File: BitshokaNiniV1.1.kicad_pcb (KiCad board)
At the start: 4 copper layers, 56.5 x 99.8 mm, 154 parts, among them J1 54-00164, J2 TC2030-IDC, J3 Conn_01x04, J4 Conn_01x06, J5 USB_C_Receptacle_USB2.0, J6 Conn_01x04, J7 Conn_01x04, Q1 MMBT3906, Q3 MMBT3906, SW1 GT-TC029B-H025-L1N, SW2 GT-TC029B-H025-L1N, T1 net-tie, U10 EMC2101, U2 TPS546D24ARVFR, U23 LM358, U3 RT9080-33GJ5, U4 ESP32-S3-WROOM-1, U5 SPX3819M5-L-1-8, U7 25MHz, U9 SN74AVC4T774

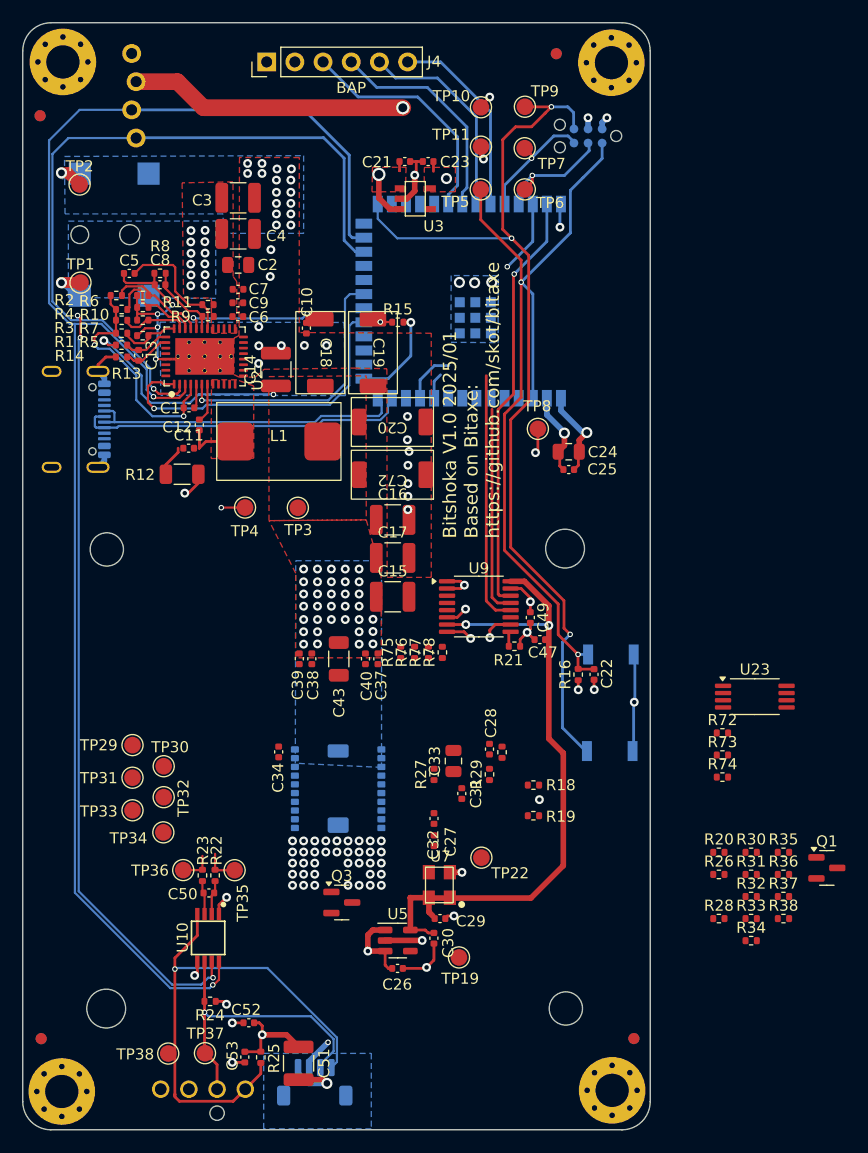
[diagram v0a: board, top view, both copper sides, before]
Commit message: All components placed
Went through TI schematic and layout checklist.
All components placed and initial DRC
Need thermal vias on KF1950 and also better layout (so not so many errors)
Need to do silk
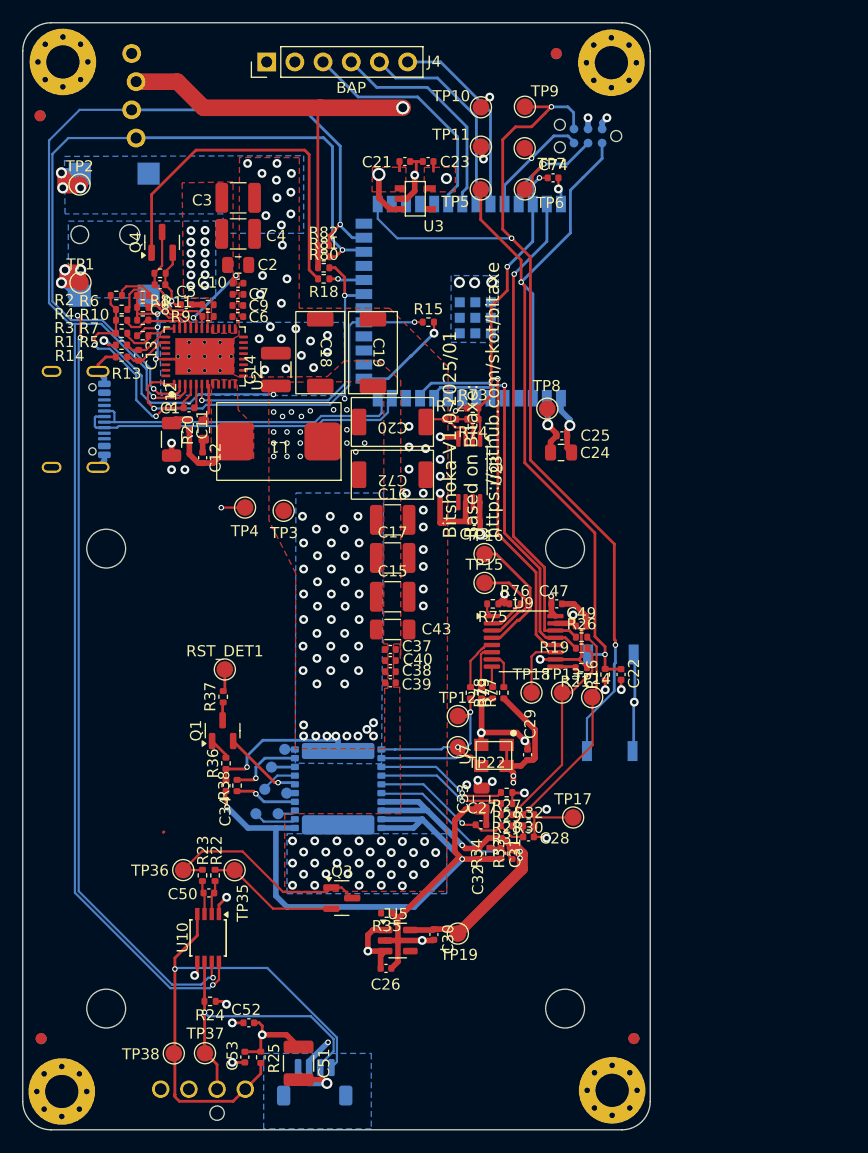
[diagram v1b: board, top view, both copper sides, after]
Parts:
- removed TP29, TP30, TP31, TP32, TP33, TP34: TestPoint, TestPoint:TestPoint_Pad_D1.5mm
- added C73: 0.1uF, Capacitor_SMD:C_0402_1005Metric, F.Cu at (117.9, 92.5)
- added C74: 0.1uF, Capacitor_SMD:C_0402_1005Metric, F.Cu at (125.0, 61.5)
- added Q4: MMBT2222A, Package_TO_SOT_SMD:SOT-23, F.Cu at (89.8, 67.3)
- added R79: 0, Resistor_SMD:R_0402_1005Metric, F.Cu at (117.5, 107.9)
- added R80: 4.7k, Resistor_SMD:R_0402_1005Metric, F.Cu at (104.3, 69.6)
- added R81: 4.7k, Resistor_SMD:R_0402_1005Metric, F.Cu at (104.3, 68.6)
- added R82: 4.7k, Resistor_SMD:R_0402_1005Metric, F.Cu at (104.3, 67.6)
- added RST_DET1: TestPoint, TestPoint:TestPoint_Pad_D1.5mm, F.Cu at (95.4, 105.8)
- added TP12: TestPoint, TestPoint:TestPoint_Pad_D1.5mm, F.Cu at (116.4, 110.0)
- added TP13: TestPoint, TestPoint:TestPoint_Pad_D1.5mm, F.Cu at (125.8, 107.9)
- added TP14: TestPoint, TestPoint:TestPoint_Pad_D1.5mm, F.Cu at (128.5, 108.3)
- added TP15: TestPoint, TestPoint:TestPoint_Pad_D1.5mm, F.Cu at (118.8, 98.0)
- added TP16: TestPoint, TestPoint:TestPoint_Pad_D1.5mm, F.Cu at (118.8, 95.4)
- added TP17: TestPoint, TestPoint:TestPoint_Pad_D1.5mm, F.Cu at (126.8, 119.1)
- added TP18: TestPoint, TestPoint:TestPoint_Pad_D1.5mm, F.Cu at (123.0, 107.9)
- added TP20: TestPoint, TestPoint:TestPoint_Pad_D1.0mm, B.Cu at (100.8, 113.0)
- added TP21: TestPoint, TestPoint:TestPoint_Pad_D1.0mm, B.Cu at (99.6, 114.6)
- added TP23: TestPoint, TestPoint:TestPoint_Pad_D1.0mm, B.Cu at (99.0, 116.6)
- added TP24: TestPoint, TestPoint:TestPoint_Pad_D1.0mm, B.Cu at (101.0, 116.9)
- added TP25: TestPoint, TestPoint:TestPoint_Pad_D1.0mm, B.Cu at (100.2, 118.8)
- added TP26: TestPoint, TestPoint:TestPoint_Pad_D1.0mm, B.Cu at (98.2, 118.8)
- R1: value 8.25k -> 4.64k
- R10: value 68.1k -> 0
- R18: value 0 -> 100
- R20: footprint Resistor_SMD:R_0402_1005Metric -> Resistor_SMD:R_0603_1608Metric
- R32: value 390 -> 400
- R33: value 27.5 -> 33
- R34: value 33 -> 27
- R5: value 14.7k -> 4.64k
- R73: value 40k -> 0
- U7: value 25MHz -> 24MHz
- moved R20 60.0 mm to (93.5, 84.2), turned to 90 degrees
- moved Q1 55.8 mm to (95.2, 111.3), turned to 90 degrees
- moved R37 53.6 mm to (95.2, 108.3), turned to 90 degrees
- moved R36 51.2 mm to (95.5, 114.3), turned to 90 degrees
- moved R38 50.7 mm to (96.5, 116.3), turned to 90 degrees
- moved R18 49.4 mm to (104.3, 70.6)
- moved R74 39.3 mm to (117.8, 83.2), turned to 180 degrees
- moved R73 38.5 mm to (117.7, 82.2)
- moved R72 37.4 mm to (115.7, 83.2)
- moved R35 36.2 mm to (110.0, 127.8), turned to 180 degrees
- moved U23 32.8 mm to (117.4, 87.9), turned to -90 degrees
- moved R34 24.8 mm to (119.3, 122.4), turned to 90 degrees
- moved R26 24.7 mm to (127.5, 102.9)
- moved R31 22.5 mm to (120.8, 119.9), turned to 180 degrees
- moved R33 22.3 mm to (121.3, 122.4), turned to 90 degrees
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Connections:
- C12 pad 1: Net-(U2-BOOT) -> Net-(C12-Pad1)
- C26 pad 2: GND -> /KF1950/LDO_GND
- C28 pad 1: /KF1950/1V8 -> GND
- C29 pad 2: /KF1950/1V2 -> /KF1950/1V8
- C30 pad 2: GND -> /KF1950/LDO_GND
- C33 pad 2: /KF1950/VDD -> /VDD
- C34 pad 2: /KF1950/VDD -> /VDD
- C37 pad 1: /KF1950/VDD -> /VDD
- C38 pad 1: /KF1950/VDD -> /VDD
- C39 pad 1: /KF1950/VDD -> /VDD
- C40 pad 1: /KF1950/VDD -> /VDD
- C43 pad 1: /KF1950/VDD -> /VDD
- R17 pad 1: /KF1950/ESP_RXD -> GND
- R17 pad 2: /KF1950/TXD -> Net-(U9-A4)
- R18 pad 1: /KF1950/TXD_1V8 -> /ESP32//TPS_EN
- R18 pad 2: /KF1950/RXD -> Net-(Q4-B)
- R19 pad 1: /KF1950/ESP_TXD -> /ESP_TXD
- R20 pad 1: /KF1950/RST_1V8 -> Net-(C12-Pad1)
- R20 pad 2: /KF1950//RST -> Net-(U2-BOOT)
- R26 pad 1: /KF1950/ESP_RST -> /ESP_RST
- R32 pad 2: /KF1950/1V8 -> GND
- R36 pad 1: /KF1950/VDD -> /VDD
- U4 pad 10: /TX -> /ESP_TXD
- U4 pad 11: /RX -> /ESP_RXD
- U4 pad 22: unconnected-(U4-GPIO14/TOUCH14/ADC2_CH3/FSPIWP/FSPIDQS/SUBSPIWP-Pad22) -> /ESP32//TPS_EN
- U4 pad 39: /RST -> /ESP_RST
- U5 pad 2: GND -> /KF1950/LDO_GND
- U7 pad 4: /KF1950/1V2 -> /KF1950/1V8
- U8 pad 12: unconnected-(U8-GND-Pad12) -> Net-(TP26-Pad1)
- U8 pad 13: unconnected-(U8-DIR-Pad13) -> Net-(TP25-Pad1)
- U8 pad 15: unconnected-(U8-0.9V-Pad15) -> Net-(TP24-Pad1)
- U8 pad 17: unconnected-(U8-RXD-Pad17) -> Net-(TP23-Pad1)
- U8 pad 18: unconnected-(U8-CTSI-Pad18) -> Net-(TP21-Pad1)
- U8 pad 20: unconnected-(U8-CLK-Pad20) -> Net-(TP20-Pad1)
- U8 pad 21: /KF1950/VDD -> /VDD
- U9 pad 11: unconnected-(U9-B4-Pad11) -> Net-(U9-B4)
- U9 pad 12: /KF1950/ESP_RXD -> /ESP_RXD
- U9 pad 13: /KF1950/ESP_TXD -> /ESP_TXD
- U9 pad 14: /KF1950/ESP_RST -> /ESP_RST
- U9 pad 6: GND -> Net-(U9-A4)
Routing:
- net /KF1950/LDO_GND: track 0.00 -> 75.8 mm, vias 0 -> 3
- net /KF1950/1V8: track 0.00 -> 74.1 mm, vias 0 -> 6
- net (no net): track 59.0 -> 0.07 mm, vias 2 -> 0
- net /ESP_RST: track 0.00 -> 43.9 mm, vias 0 -> 1
- net /VDD: track 20.1 -> 62.7 mm, vias 36 -> 73
- net /RST: track 38.2 -> 0.00 mm, vias 1 -> 0
- net /ESP_RXD: track 0.00 -> 34.6 mm, vias 0 -> 1
- net /ESP_TXD: track 0.00 -> 34.4 mm, vias 0 -> 1
- net Net-(Q4-B): track 0.00 -> 32.8 mm
- net GND: track 71.9 -> 94.9 mm, vias 93 -> 102
- net /KF1950/ESP_RXD: track 22.8 -> 0.00 mm
- net /KF1950//RST: track 0.00 -> 20.5 mm
- net Net-(U4-GPIO2/TOUCH2/ADC1_CH1): track 6.63 -> 26.6 mm, vias 1 -> 2
- net /KF1950/ESP_TXD: track 18.8 -> 0.00 mm
- net /KF1950/RXD: track 0.04 -> 18.6 mm
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- added copper zone on In2.Cu, net /VDD
- added copper zone on B.Cu, net unconnected-(J7-MountPin-PadMP)
- removed copper zone on B.Cu, net unconnected-(J7-MountPin-PadMP)_1
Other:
- board text added: "This area is solder mask free for heatsinking with 14 x 14mm Raspberry PI heatsink"

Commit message: Silk Done
Still need to fix up heatsink vias on ASIC and paste layer for thermal
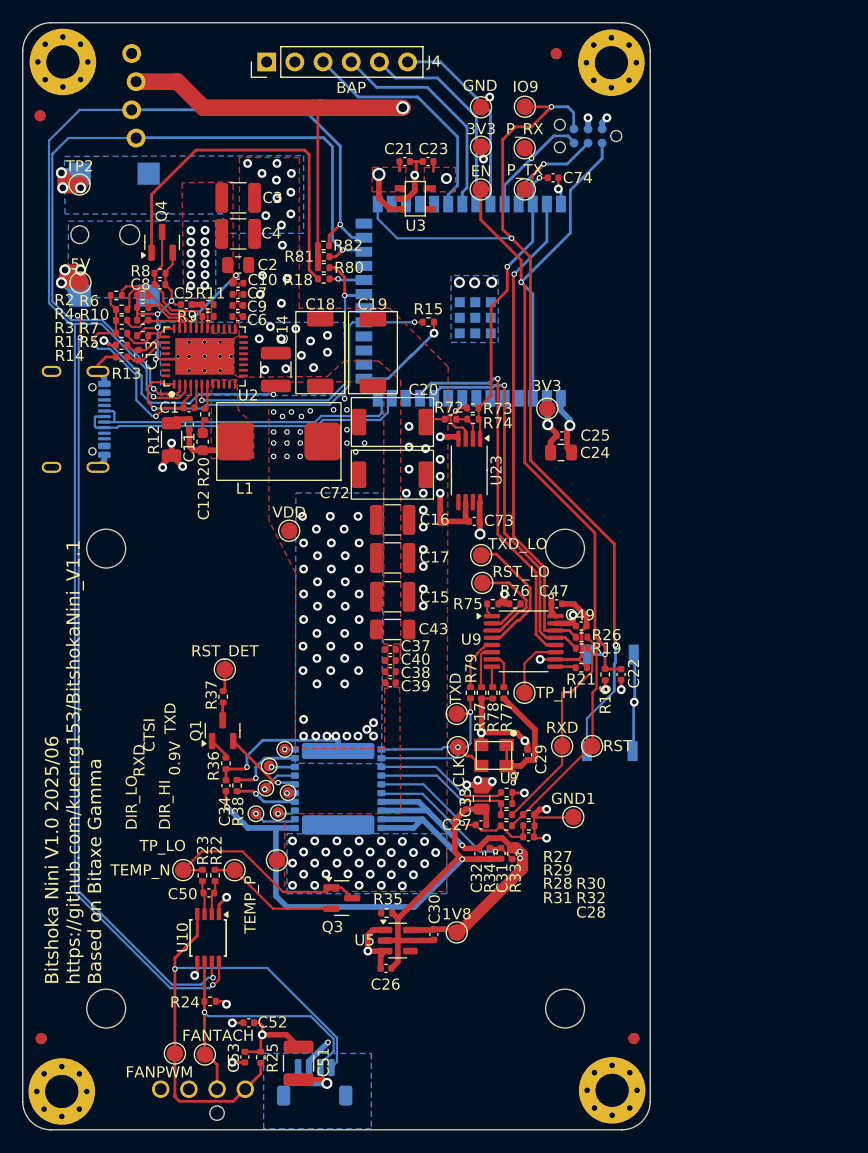
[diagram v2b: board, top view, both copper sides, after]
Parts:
- removed TP12, TP13, TP14, TP15, TP16, TP17, TP18, TP19, TP3, TP37, TP38, TP4: TestPoint, TestPoint:TestPoint_Pad_D1.5mm
- removed TP20, TP21, TP23, TP24, TP25, TP26: TestPoint, TestPoint:TestPoint_Pad_D1.0mm
- added 0.9V: TestPoint, TestPoint:TestPoint_Pad_D1.0mm, F.Cu at (101.1, 116.9)
- added 1V8: TestPoint, TestPoint:TestPoint_Pad_D1.5mm, F.Cu at (116.3, 129.5)
- added CTSI: TestPoint, TestPoint:TestPoint_Pad_D1.0mm, F.Cu at (99.4, 114.5)
- added DIR_HI: TestPoint, TestPoint:TestPoint_Pad_D1.0mm, F.Cu at (100.2, 118.7)
- added DIR_LO: TestPoint, TestPoint:TestPoint_Pad_D1.0mm, F.Cu at (98.2, 118.8)
- added FANPWM: TestPoint, TestPoint:TestPoint_Pad_D1.5mm, F.Cu at (90.9, 140.4)
- added FANTACH: TestPoint, TestPoint:TestPoint_Pad_D1.5mm, F.Cu at (93.6, 140.5)
- added GND1: TestPoint, TestPoint:TestPoint_Pad_D1.5mm, F.Cu at (126.8, 119.1)
- added RST: TestPoint, TestPoint:TestPoint_Pad_D1.5mm, F.Cu at (128.5, 112.7)
- added RST_LO: TestPoint, TestPoint:TestPoint_Pad_D1.5mm, F.Cu at (118.6, 98.0)
- added RXD: TestPoint, TestPoint:TestPoint_Pad_D1.0mm, F.Cu at (99.1, 116.5)
- added RXD: TestPoint, TestPoint:TestPoint_Pad_D1.5mm, F.Cu at (125.8, 112.7)
- added TP_HI: TestPoint, TestPoint:TestPoint_Pad_D1.5mm, F.Cu at (122.4, 107.9)
- added TP_LO: TestPoint, TestPoint:TestPoint_Pad_D1.5mm, F.Cu at (100.1, 123.0)
- added TXD: TestPoint, TestPoint:TestPoint_Pad_D1.0mm, F.Cu at (100.8, 113.0)
- added TXD: TestPoint, TestPoint:TestPoint_Pad_D1.5mm, F.Cu at (116.3, 109.8)
- added TXD_LO: TestPoint, TestPoint:TestPoint_Pad_D1.5mm, F.Cu at (118.5, 95.5)
- added VDD: TestPoint, TestPoint:TestPoint_Pad_D1.5mm, F.Cu at (101.2, 93.3)
- C12: footprint Capacitor_SMD:C_0402_1005Metric -> Capacitor_SMD:C_0603_1608Metric
- R20: footprint Resistor_SMD:R_0603_1608Metric -> Resistor_SMD:R_0402_1005Metric
- U8: value ~ -> KF1950
- moved C12 1.44 mm to (93.4, 85.3)
- moved R20 1.42 mm to (93.6, 82.8)
- renumbered TP8 to 3V3, TP11 to 3V3, TP1 to 5V, TP22 to CLK, TP5 to EN, TP10 to GND, TP9 to IO9, TP7 to P_RX, TP6 to P_TX, RST_DET1 to RST_DET, TP36 to TEMP_N, TP35 to TEMP_P
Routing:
- net /VDD: track 62.7 -> 66.5 mm
- net GND: track 94.9 -> 96.9 mm, vias 102 -> 101
- net /Power/SW: track 9.72 -> 8.35 mm
- net Net-(U2-BOOT): track 3.55 -> 2.31 mm
- net Net-(TXD2-Pad1): vias 0 -> 1
- net Net-(RXD2-Pad1): vias 0 -> 1
- net Net-(DIR_LO1-Pad1): vias 0 -> 1
- net Net-(DIR_HI1-Pad1): vias 0 -> 1
- net Net-(CTSI1-Pad1): vias 0 -> 1
- net Net-(0.9V1-Pad1): vias 0 -> 1
- net /KF1950/LDO_GND: vias 3 -> 2
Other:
- board text added: "Bitshoka Nini V1.0 2025/06 https://github.com/kuenrg153/BitshokaNini_V1.1 Based on Bitaxe Gamma"
- board text removed: "/ 21M"
- board text removed: "Bitshoka V1.0 2025/01 Based on Bitaxe: https://github.com/skot/bitaxe"
- board text removed: "∞"

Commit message: PCB fixes
Fixed up KF1950 footprint
Added heatsinking to the bottom
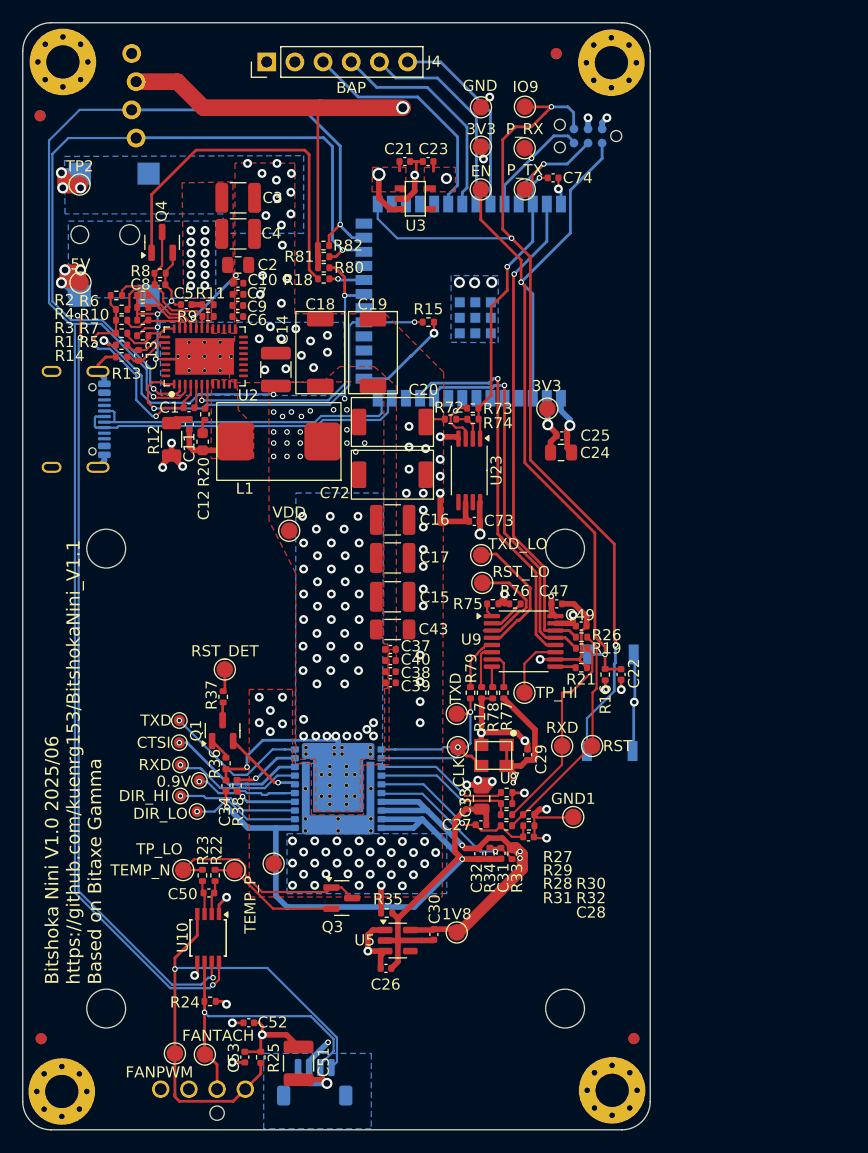
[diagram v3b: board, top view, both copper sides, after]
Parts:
- moved TXD 9.85 mm to (91.3, 110.4)
- moved DIR_HI 8.93 mm to (91.4, 117.2)
- moved CTSI 8.37 mm to (91.3, 112.4)
- moved 0.9V 8.08 mm to (93.1, 115.8)
- moved RXD 7.98 mm to (91.4, 114.4)
- moved DIR_LO 5.30 mm to (92.9, 118.6)
- moved TP_LO 0.42 mm to (99.8, 123.3)
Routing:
- net Net-(TXD2-Pad1): track 0.92 -> 13.4 mm
- net Net-(CTSI1-Pad1): track 2.12 -> 12.6 mm
- net Net-(0.9V1-Pad1): track 0.74 -> 10.9 mm
- net Net-(DIR_HI1-Pad1): track 1.63 -> 10.9 mm
- net Net-(RXD2-Pad1): track 3.29 -> 11.6 mm
- net Net-(DIR_LO1-Pad1): track 3.89 -> 9.85 mm
- net GND: track 96.9 -> 99.4 mm, vias 101 -> 111
- net Net-(R38-Pad2): track 6.61 -> 6.02 mm
